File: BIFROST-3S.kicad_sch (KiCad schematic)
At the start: 6 parts, among them J1 1-776267-1, J2 200241-1222, J3 200241-1222, J4 B6B-XH-A_LF__SN_, J5 B4B-XH-A_LF__SN_

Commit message: Schematic+Layout 2.0
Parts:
- removed J1: 1-776267-1, 1-776267-1:17762671, symbol 1-776267-1:1-776267-1
- added J6: 560020-1020, 560020-1020:5600201020, symbol 560020-1020:560020-1020
- added J7: 200241-1222, 200241-1222:2002411222, symbol 200241-1222:200241-1222
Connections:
- net BAT1: now also J6.2
- net BAT2: now also J6.3
- net BAT3: now also J6.4
- net BQ2_TS1: now also J6.10
- net BQ2_TS2: now also J6.9
- net BQ2_TS3: now also J6.8
- net BQ_TS: now also J6.5
- net GND: now also J6.1, J6.6, J6.7, J7.1
- net PACK+_RAW: now also J7.2

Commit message: Schematic+Layout 3.0
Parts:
- removed J2: 200241-1222, 200241-1222:2002411222, symbol 200241-1222:200241-1222
- added F1: MF-RHS800-0, MF-RHS800-0:MFRHS8000, symbol MF-RHS800-0:MF-RHS800-0
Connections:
- net +BATT: now also F1.2
- net PACK+_RAW: now also F1.1
- net BAT3 renamed BAT3/PACK+
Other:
- moved on the sheet: J3

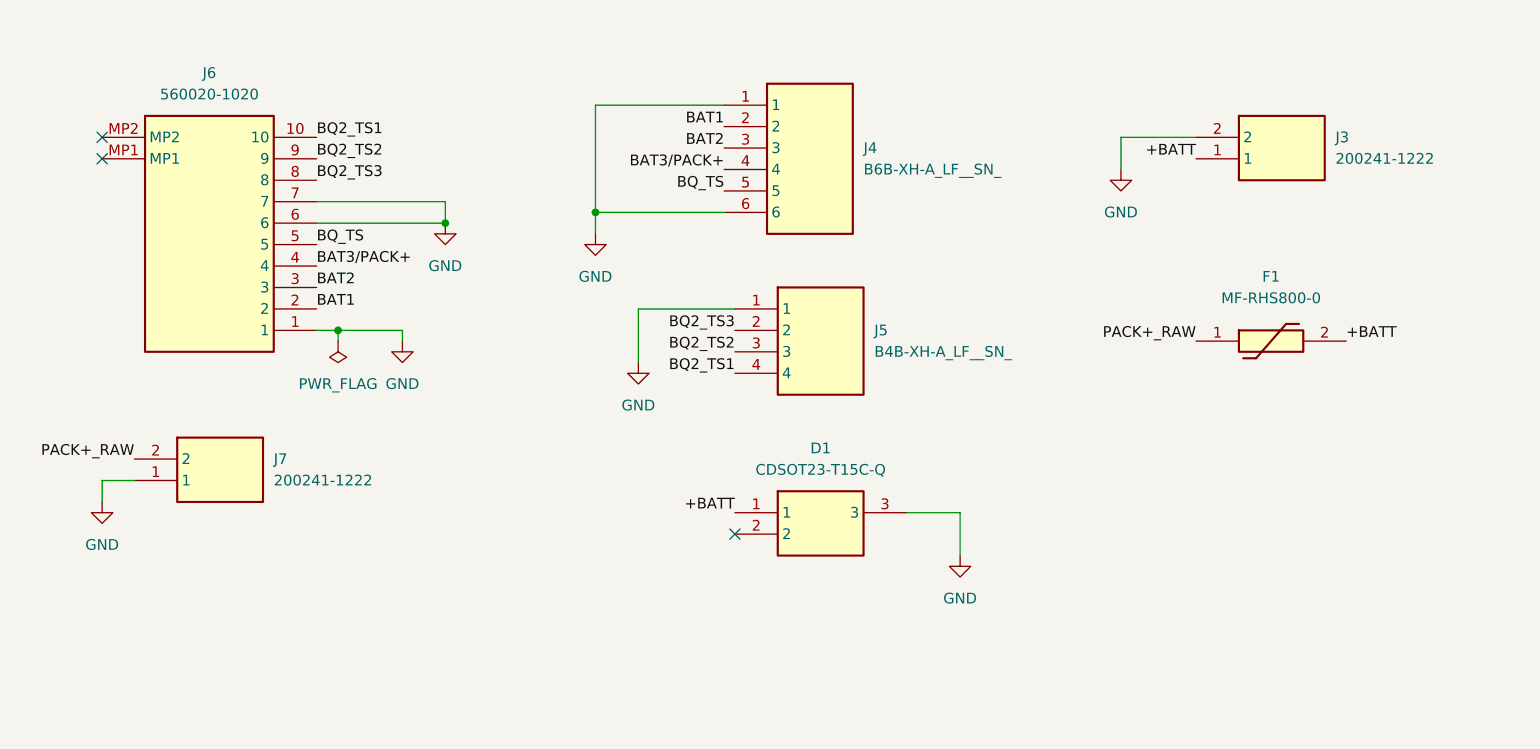
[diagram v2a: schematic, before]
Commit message: Finalized Silkscreen
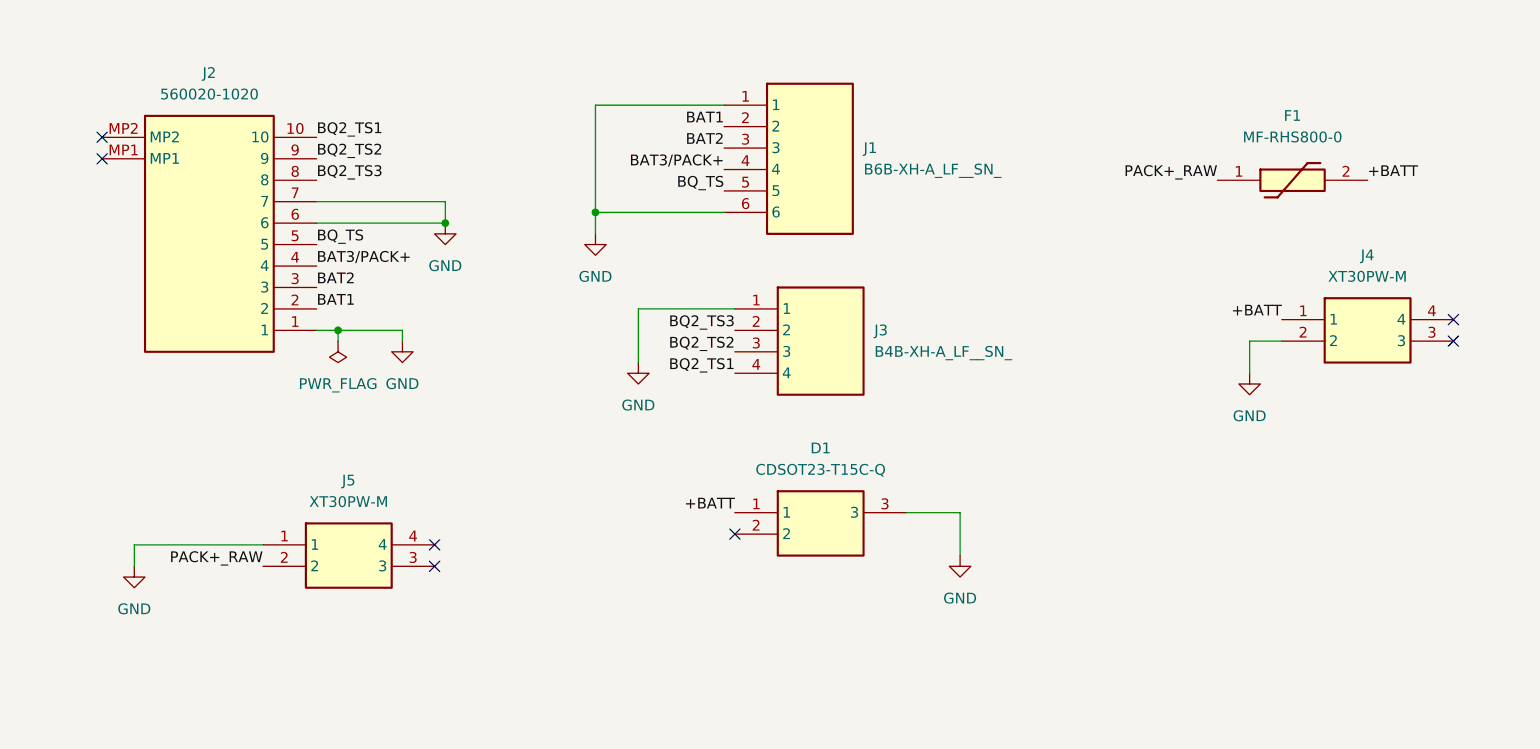
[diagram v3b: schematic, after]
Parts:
- removed J3, J7: 200241-1222, 200241-1222:2002411222, symbol 200241-1222:200241-1222
- added J4, J5: XT30PW-M, XT30PW-M:XT30PWM, symbol XT30PW-M:XT30PW-M
- renumbered J4 to J1, J6 to J2, J5 to J3
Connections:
- net +BATT: now also J4.1
- net GND: now also J4.2, J5.1
- net PACK+_RAW: now also J5.2
- no-connect marks 3 -> 7
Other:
- moved on the sheet: F1

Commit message: Layout 3.1
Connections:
- net +BATT: now also J4.2; no longer J4.1
- net GND: now also J4.1; no longer J4.2
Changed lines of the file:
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@@
-	(wire
-		(pts
-			(xy 161.29 50.8) (xy 161.29 54.61)
-		)
-		(stroke
-			(width 0)
-			(type default)
-		)
-	)
 	(wire
 		(pts
@@
 	(wire
 		(pts
+			(xy 157.48 48.26) (xy 157.48 53.34)
+		)
+		(stroke
+			(width 0)
+			(type default)
+		)
+	)
+	(wire
+		(pts
 			(xy 60.96 49.53) (xy 60.96 50.8)
 		)
@@
 	(wire
 		(pts
-			(xy 165.1 50.8) (xy 161.29 50.8)
+			(xy 165.1 48.26) (xy 157.48 48.26)
 		)
 		(stroke
@@
 	)
 	(label "+BATT"
-		(at 165.1 48.26 180)
+		(at 165.1 50.8 180)
 		(effects
 			(font
@@
 	)
 	(symbol
-		(lib_id "power:GND")
-		(at 161.29 54.61 0)
-		(unit 1)
-		(exclude_from_sim no)
-		(in_bom yes)
-		(on_board yes)
-		(dnp no)
-		(fields_autoplaced yes)
-		(property "Reference" "#PWR04"
-			(at 161.29 60.96 0)
-			(effects
-				(font
-					(size 1.27 1.27)
-				)
-				(hide yes)
-			)
-		)
-		(property "Value" "GND"
-			(at 161.29 59.69 0)
-			(effects
-				(font
-					(size 1.27 1.27)
-				)
-			)
-		)
-		(property "Footprint" ""
-			(at 161.29 54.61 0)
-			(effects
-				(font
-					(size 1.27 1.27)
-				)
-				(hide yes)
-			)
-		)
-		(property "Datasheet" ""
-			(at 161.29 54.61 0)
-			(effects
-				(font
-					(size 1.27 1.27)
-				)
-				(hide yes)
-			)
-		)
-		(property "Description" "Power symbol creates a global label with name \"GND\" , ground"
-			(at 161.29 54.61 0)
-			(effects
-				(font
-					(size 1.27 1.27)
-				)
-				(hide yes)
-			)
-		)
-		(pin "1"
-		)
-		(instances
-			(project "BIFROST-3S"
-				(path "/61c97717-af7f-401d-a26a-01242b2529ed"
-					(reference "#PWR04")
-					(unit 1)
-				)
-			)
-		)
-	)
-	(symbol
 		(lib_id "XT30PW-M:XT30PW-M")
 		(at 44.45 74.93 0)
@@
 					(unit 1)
 				)
+			)
+		)
+	)
+	(symbol
+		(lib_id "power:GND")
+		(at 157.48 53.34 0)
+		(unit 1)
+		(exclude_from_sim no)
+		(in_bom yes)
+		(on_board yes)
+		(dnp no)
+		(fields_autoplaced yes)
+		(property "Reference" "#PWR04"
+			(at 157.48 59.69 0)
+			(effects
+				(font
+					(size 1.27 1.27)
+				)
+				(hide yes)
+			)
+		)
+		(property "Value" "GND"
+			(at 157.48 58.42 0)
+			(effects
+				(font
+					(size 1.27 1.27)
+				)
+			)
+		)
+		(property "Footprint" ""
+			(at 157.48 53.34 0)
+			(effects
+				(font
+					(size 1.27 1.27)
+				)
+				(hide yes)
+			)
+		)
+		(property "Datasheet" ""
+			(at 157.48 53.34 0)
+			(effects
+				(font
+					(size 1.27 1.27)
+				)
+				(hide yes)
+			)
+		)
+		(property "Description" "Power symbol creates a global label with name \"GND\" , ground"
+			(at 157.48 53.34 0)
+			(effects
+				(font
+					(size 1.27 1.27)
+				)
+				(hide yes)
+			)
+		)
+		(pin "1"
+		)
+		(instances
+			(project "BIFROST-3S"
+				(path "/61c97717-af7f-401d-a26a-01242b2529ed"
+					(reference "#PWR04")
+					(unit 1)
+				)

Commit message: Layout 4.0
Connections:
- net +BATT: now also J4.1; no longer J4.2
- net GND: now also J4.2; no longer J4.1
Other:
- note added: "Power Input"
- note added: "Power Output"
- note added: "Signal Input"
- note added: "Signal Output"
- note added: "System Protection"
- moved on the sheet: D1, F1, J1, J2, J3, J4, J5

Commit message: Schematic+Layout 5.0
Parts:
- removed J2: 560020-1020, 560020-1020:5600201020, symbol 560020-1020:560020-1020
- removed J5: XT30PW-M, XT30PW-M:XT30PWM, symbol XT30PW-M:XT30PW-M
- added J2: Conn_01x12, Bifrost_Wire_Pads:Bifrost_Wire_Pads, symbol Connector_Generic:Conn_01x12
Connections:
- net BAT1: now also J2.2 (Pin_2)
- net BAT2: now also J2.3 (Pin_3)
- net BAT3/PACK+: now also J2.4 (Pin_4)
- net BQ2_TS1: now also J2.10 (Pin_10)
- net BQ2_TS2: now also J2.9 (Pin_9)
- net BQ2_TS3: now also J2.8 (Pin_8)
- net BQ_TS: now also J2.5 (Pin_5)
- net GND: now also J2.1 (Pin_1), J2.11 (Pin_11), J2.6 (Pin_6), J2.7 (Pin_7)
- net PACK+_RAW: now also J2.12 (Pin_12)
- no-connect marks 7 -> 3
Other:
- note removed: "Power Input"
- note removed: "Signal Input"
- moved on the sheet: D1, F1, J1, J3, J4

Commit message: Layout 5.2
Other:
- moved on the sheet: D1, J2, J4

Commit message: New Fuse+Gerbers
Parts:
- removed F1: MF-RHS800-0, MF-RHS800-0:MFRHS8000, symbol MF-RHS800-0:MF-RHS800-0
- added F1: SF-1206HHA800R-2, SF-1206HHA800R-2:SF1206HHA800R2, symbol SF-1206HHA800R-2:SF-1206HHA800R-2
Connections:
- net +BATT: now also F1.2
- net PACK+_RAW: now also F1.1
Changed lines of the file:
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@@
-	)
-	(symbol
-		(lib_id "MF-RHS800-0:MF-RHS800-0")
-		(at 107.95 26.67 0)
-		(unit 1)
-		(exclude_from_sim no)
-		(in_bom yes)
-		(on_board yes)
-		(dnp no)
-		(fields_autoplaced yes)
-		(property "Reference" "F1"
-			(at 116.84 19.05 0)
-			(effects
-				(font
-					(size 1.27 1.27)
-				)
-			)
-		)
-		(property "Value" "MF-RHS800-0"
-			(at 116.84 21.59 0)
-			(effects
-				(font
-					(size 1.27 1.27)
-				)
-			)
-		)
-		(property "Footprint" "MF-RHS800-0:MFRHS8000"
-			(at 121.92 122.86 0)
-			(effects
-				(font
-					(size 1.27 1.27)
-				)
-				(justify left top)
-				(hide yes)
-			)
-		)
-		(property "Datasheet" "https://www.bourns.com/docs/Product-Datasheets/MF-RHS.pdf"
-			(at 121.92 222.86 0)
-			(effects
-				(font
-					(size 1.27 1.27)
-				)
-				(justify left top)
-				(hide yes)
-			)
-		)
-		(property "Description" "PTC 8.0A 16V RADIAL LEADED HI-TEMP"
-			(at 107.95 26.67 0)
-			(effects
-				(font
-					(size 1.27 1.27)
-				)
-				(hide yes)
-			)
-		)
-		(property "Height" "24.7"
-			(at 121.92 422.86 0)
-			(effects
-				(font
-					(size 1.27 1.27)
-				)
-				(justify left top)
-				(hide yes)
-			)
-		)
-		(property "Mouser Part Number" "652-MF-RHS800-0"
-			(at 121.92 522.86 0)
-			(effects
-				(font
-					(size 1.27 1.27)
-				)
-				(justify left top)
-				(hide yes)
-			)
-		)
-		(property "Mouser Price/Stock" "https://www.mouser.co.uk/ProductDetail/Bourns/MF-RHS800-0?qs=mELouGlnn3db4Obe02aVdw%3D%3D"
-			(at 121.92 622.86 0)
-			(effects
-				(font
-					(size 1.27 1.27)
-				)
-				(justify left top)
-				(hide yes)
-			)
-		)
-		(property "Manufacturer_Name" "Bourns"
-			(at 121.92 722.86 0)
-			(effects
-				(font
-					(size 1.27 1.27)
-				)
-				(justify left top)
-				(hide yes)
-			)
-		)
-		(property "Manufacturer_Part_Number" "MF-RHS800-0"
-			(at 121.92 822.86 0)
-			(effects
-				(font
-					(size 1.27 1.27)
-				)
-				(justify left top)
-				(hide yes)
-			)
-		)
-		(pin "1"
-		)
-		(pin "2"
-		)
-		(instances
-			(project ""
-				(path "/61c97717-af7f-401d-a26a-01242b2529ed"
-					(reference "F1")
-					(unit 1)
-				)
-			)
-		)
 	)
 	(symbol
@@
 					(unit 1)
 				)
+			)
+		)
+	)
+	(symbol
+		(lib_id "SF-1206HHA800R-2:SF-1206HHA800R-2")
+		(at 107.95 26.67 0)
+		(unit 1)
+		(exclude_from_sim no)
+		(in_bom yes)
+		(on_board yes)
+		(dnp no)
+		(fields_autoplaced yes)
+		(property "Reference" "F1"
+			(at 116.84 20.32 0)
+			(effects
+				(font
+					(size 1.27 1.27)
+				)
+			)
+		)
+		(property "Value" "SF-1206HHA800R-2"
+			(at 116.84 22.86 0)
+			(effects
+				(font
+					(size 1.27 1.27)
+				)
+			)
+		)
+		(property "Footprint" "SF-1206HHA800R-2:SF1206HHA800R2"
+			(at 121.92 122.86 0)
+			(effects
+				(font
+					(size 1.27 1.27)
+				)
+				(justify left top)
+				(hide yes)
+			)
+		)
+		(property "Datasheet" "https://www.bourns.com/docs/Product-Datasheets/SF-1206HHA-R.pdf"
+			(at 121.92 222.86 0)
+			(effects
+				(font
+					(size 1.27 1.27)
+				)
+				(justify left top)
+				(hide yes)
+			)
+		)
+		(property "Description" "1206 high-current met-foil. 8A Auto"
+			(at 107.95 26.67 0)
+			(effects
+				(font
+					(size 1.27 1.27)
+				)
+				(hide yes)
+			)
+		)
+		(property "Height" "1.2"
+			(at 121.92 422.86 0)
+			(effects
+				(font
+					(size 1.27 1.27)
+				)
+				(justify left top)
+				(hide yes)
+			)
+		)
+		(property "Mouser Part Number" "652-SF-1206HHA800R-2"
+			(at 121.92 522.86 0)
+			(effects
+				(font
+					(size 1.27 1.27)
+				)
+				(justify left top)
+				(hide yes)
+			)
+		)
+		(property "Mouser Price/Stock" "https://www.mouser.co.uk/ProductDetail/Bourns/SF-1206HHA800R-2?qs=Imq1NPwxi77tr2%2FYGnM5Ig%3D%3D"
+			(at 121.92 622.86 0)
+			(effects
+				(font
+					(size 1.27 1.27)
+				)
+				(justify left top)
+				(hide yes)
+			)
+		)
+		(property "Manufacturer_Name" "Bourns"
+			(at 121.92 722.86 0)
+			(effects
+				(font
+					(size 1.27 1.27)
+				)
+				(justify left top)
+				(hide yes)
+			)
+		)
+		(property "Manufacturer_Part_Number" "SF-1206HHA800R-2"
+			(at 121.92 822.86 0)
+			(effects
+				(font
+					(size 1.27 1.27)
+				)
+				(justify left top)
+				(hide yes)
+			)
+		)
+		(pin "1"
+		)
+		(pin "2"
+		)
+		(instances
+			(project ""
+				(path "/61c97717-af7f-401d-a26a-01242b2529ed"
+					(reference "F1")
+					(unit 1)
+				)
